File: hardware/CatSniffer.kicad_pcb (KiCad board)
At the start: 4 copper layers, 81 x 20 mm, 100 parts, among them J1 Antenna, J3 Conn_01x06_Female, P1 USB_C_Plug_USB2.0, SW1 SW, U1 AP2112K-3.3, U2 RFSW8006QTR7, U3 RP2040, U4 0900PC15A0036, U5 0900FM15D0039, U6 PE42421, U7 SX1262IMLTRT, U8 CC1352P1F3RGZT, U9 W25Q16JV, Y1 48MHz, Y2 32.768kHz, Y3 32Mhz, Y4 12MHz

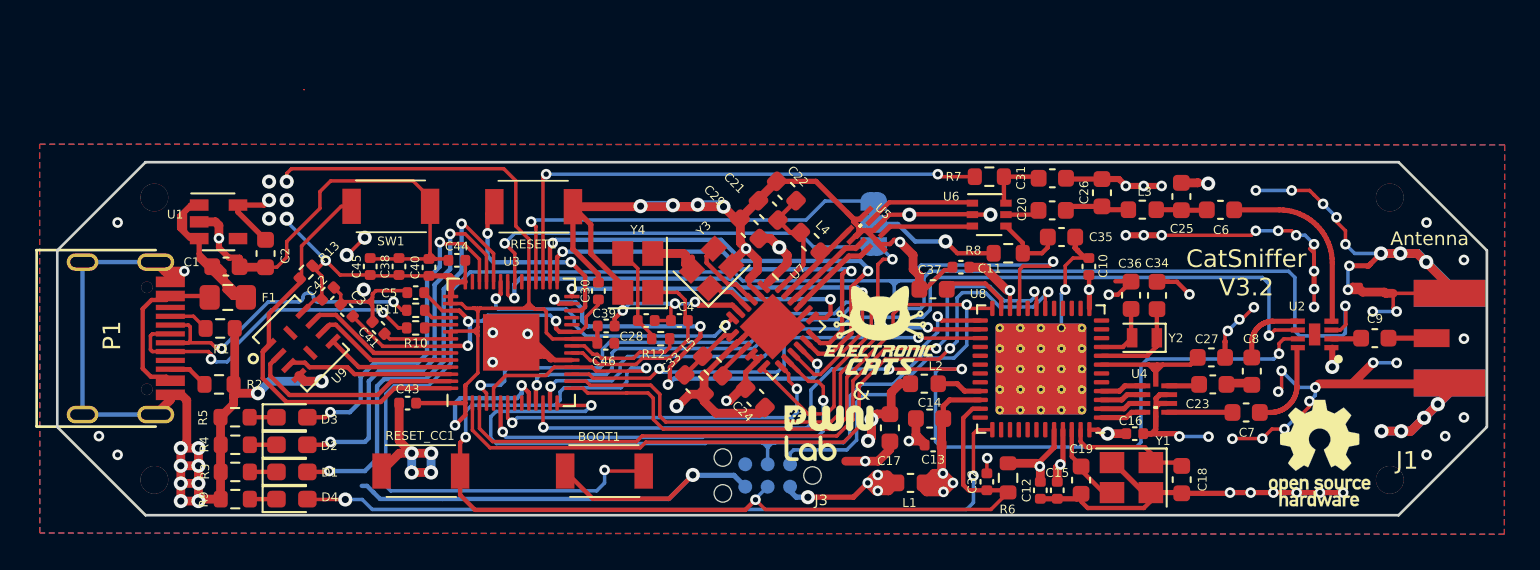
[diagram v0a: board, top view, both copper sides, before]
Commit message: Feat(Hw):Changed_antenna_switch
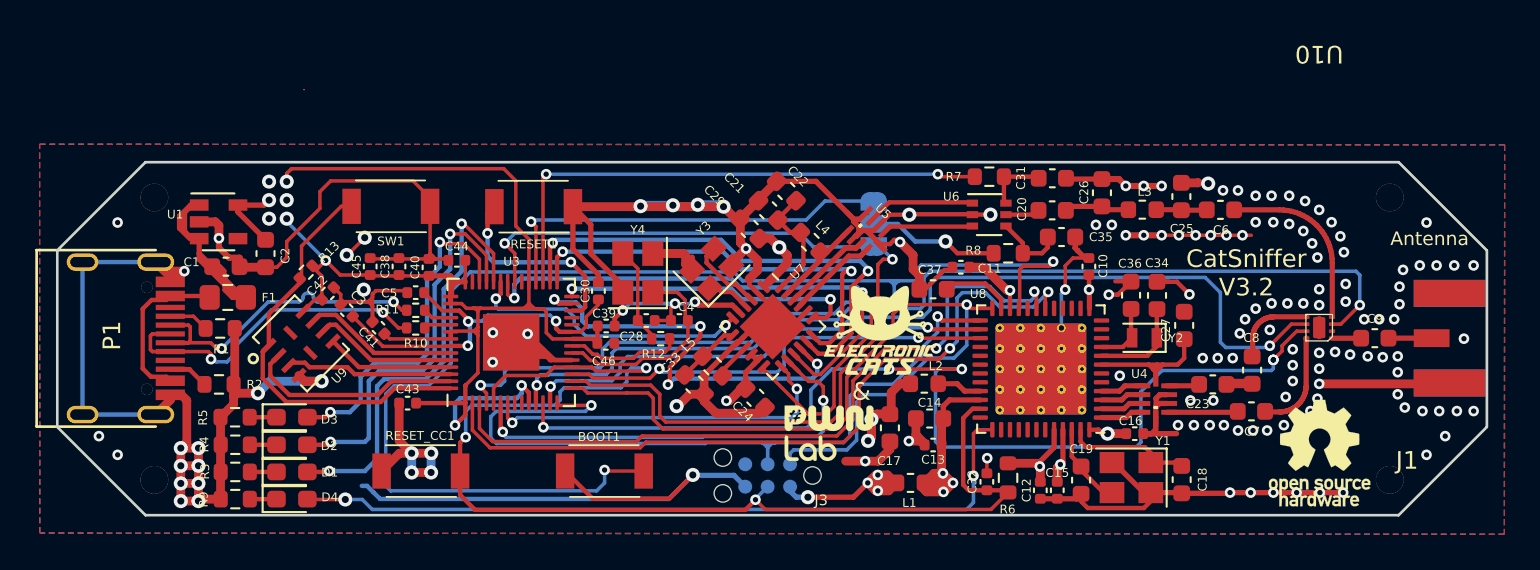
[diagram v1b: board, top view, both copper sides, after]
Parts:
- removed U2: RFSW8006QTR7, CatSniffer:SON50P200X200X90-9N
- added U10: SKY13317-373LF, CatSniffer:SKY13317-373LF, F.Cu at (156.5, 109.4)
- L1: value BLM18HE152SN1D -> BLM18HE152SN1D
- U8: value CC1352P1F3RGZT -> CC1352P74T0RGZR
- moved C27 2.38 mm to (148.8, 109.2), turned to -90 degrees
- moved C7 0.31 mm to (152.7, 114.1)
- moved C8 0.06 mm to (152.7, 111.8)
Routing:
- net GND: track 425.9 -> 353.8 mm, vias 101 -> 141
- net /CTF1: track 58.6 -> 56.4 mm
- net /CTF3: track 50.8 -> 52.0 mm
- net +3V3: track 101.1 -> 100.0 mm, vias 16 -> 15
- net Net-(U10-RF3): track 5.13 -> 5.88 mm
- net /CTF2: vias 4 -> 5

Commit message: Feat(Hw):changed_switch_capacitors_to_47uf
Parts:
- C6, C7, C8: value 100pF -> 47pF
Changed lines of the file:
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@@
 			)
 		)
-		(property "Value" "100pF"
+		(property "Value" "47pF"
 			(at 0 1.43 0)
 			(layer "F.Fab")
@@
 			)
 		)
-		(property "LCSC#" "C14858"
+		(property "LCSC#" "C519486"
 			(at 0 0 0)
 			(layer "F.Fab")
@@
 			)
 		)
-		(property "Value" "100pF"
+		(property "Value" "47pF"
 			(at 0 1.43 0)
 			(layer "F.Fab")
@@
 			)
 		)
-		(property "LCSC#" "C14858"
+		(property "LCSC#" "C519486"
 			(at 0 0 0)
 			(layer "F.Fab")
@@
 			)
 		)
-		(property "Value" "100pF"
+		(property "Value" "47pF"
 			(at 0 1.43 90)
 			(layer "F.Fab")
@@
 			)
 		)
-		(property "LCSC#" "C14858"
+		(property "LCSC#" "C519486"
 			(at 264.52 -40.84 0)
 			(layer "F.Fab")

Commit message: fix(Hw):changed_label_to_3.3v
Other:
- board text added: "CatSniffer V3.3"
- board text added: "CatSniffer v3.3"
- board text removed: "CatSniffer V3.2"
- board text removed: "CatSniffer v3.2"
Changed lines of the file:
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@@
 		)
 	)
-	(gr_text "CatSniffer\nV3.2"
+	(gr_text "CatSniffer\nV3.3"
 		(at 152.37 106.28 0)
 		(layer "F.SilkS")
@@
 		)
 	)
-	(gr_text "CatSniffer\nv3.2"
+	(gr_text "CatSniffer\nv3.3"
 		(at 98.298 110.236 0)
 		(layer "B.SilkS")
